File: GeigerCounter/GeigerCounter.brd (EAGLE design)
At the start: 100 x 80 mm, 0 parts

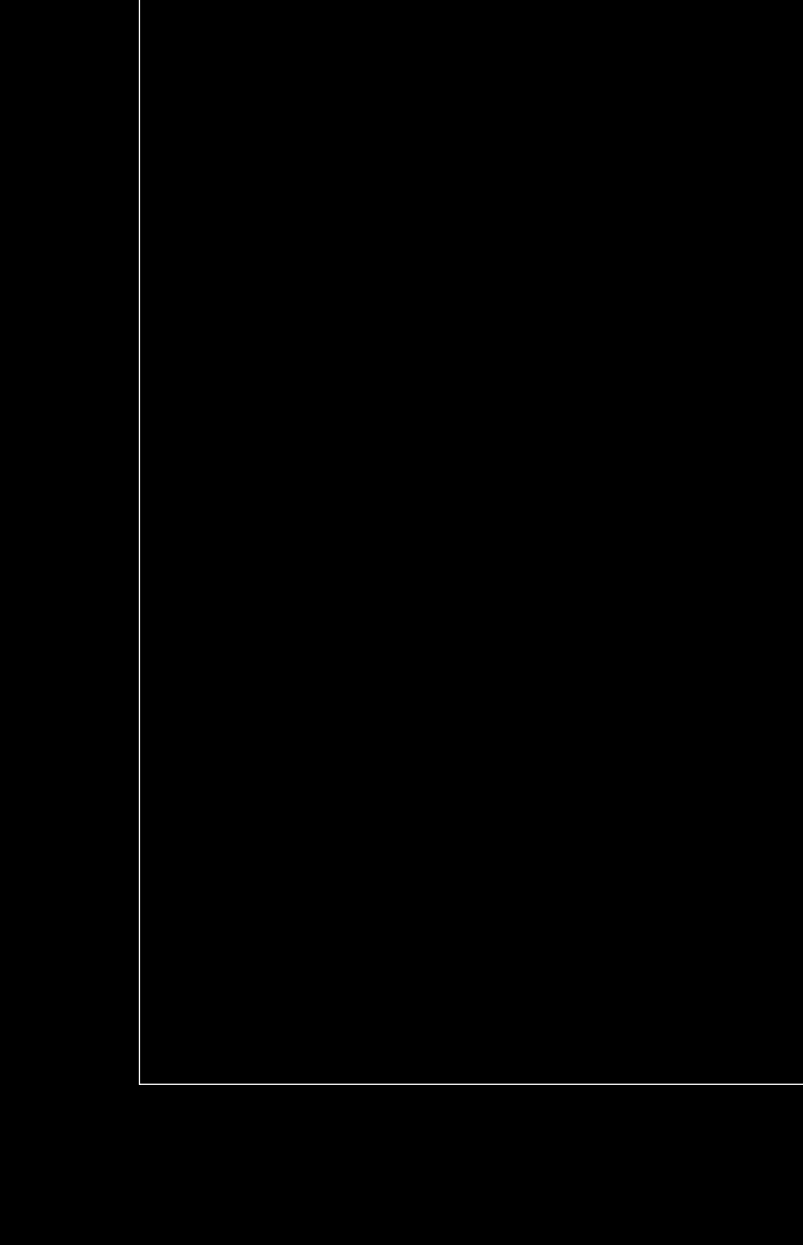
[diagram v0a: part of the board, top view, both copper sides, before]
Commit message: Added components and libraries that will be used in the project. I am using a generic op amp footprint, but made a custom photodiode footprint. I am using through hole caps and resistors throughout.
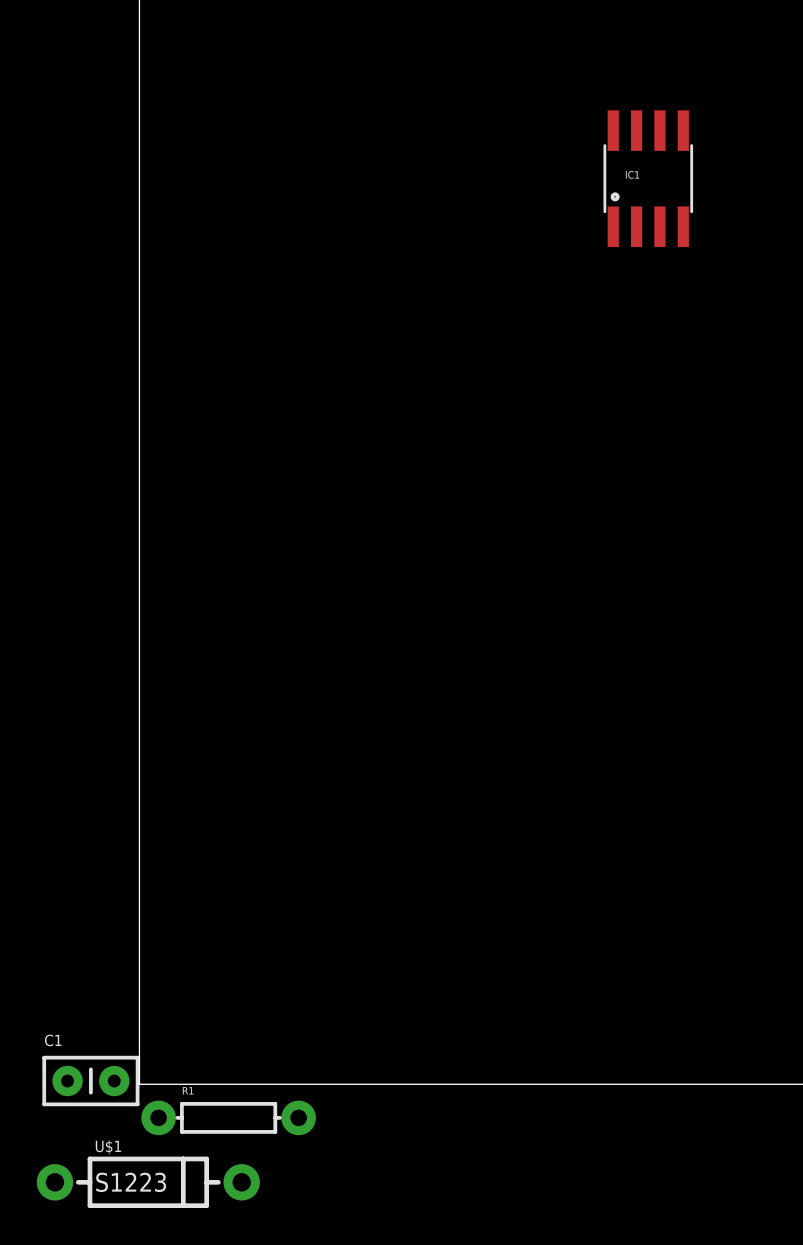
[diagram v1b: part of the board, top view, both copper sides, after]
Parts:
- added C1: (no value), SparkFun-Passives:CAP-PTH-SMALL2
- added IC1: OPAMP-DUALU, SparkFun-AnalogIC:SO08
- added R1: (no value), SparkFun-Passives:AXIAL-0.3
- added U$1: S1223, GeigerCounter:DIODE-1N4001
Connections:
- new net V+: IC1.8
- new net V-: IC1.4
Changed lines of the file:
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@@
 <setting verticaltext="up"/>
 </settings>
-<grid distance="0.05" unitdist="inch" unit="inch" style="lines" multiple="1" display="no" altdistance="0.025" altunitdist="inch" altunit="inch"/>
+<grid distance="0.001" unitdist="inch" unit="inch" style="lines" multiple="1" display="yes" altdistance="0.025" altunitdist="inch" altunit="inch"/>
 <layers>
 <layer number="1" name="Top" color="4" fill="1" visible="yes" active="yes"/>
@@
 <layer number="48" name="Document" color="7" fill="1" visible="yes" active="yes"/>
 <layer number="49" name="Reference" color="7" fill="1" visible="yes" active="yes"/>
+<layer number="50" name="dxf" color="7" fill="1" visible="no" active="no"/>
 <layer number="51" name="tDocu" color="7" fill="1" visible="yes" active="yes"/>
 <layer number="52" name="bDocu" color="7" fill="1" visible="yes" active="yes"/>
+<layer number="53" name="tGND_GNDA" color="7" fill="9" visible="no" active="no"/>
+<layer number="54" name="bGND_GNDA" color="1" fill="9" visible="no" active="no"/>
+<layer number="56" name="wert" color="7" fill="1" visible="no" active="no"/>
 <layer number="91" name="Nets" color="2" fill="1" visible="no" active="no"/>
 <layer number="92" name="Busses" color="1" fill="1" visible="no" active="no"/>
@@
 <layer number="97" name="Info" color="7" fill="1" visible="no" active="no"/>
 <layer number="98" name="Guide" color="6" fill="1" visible="no" active="no"/>
+<layer number="100" name="Muster" color="7" fill="1" visible="no" active="no"/>
+<layer number="101" name="Patch_Top" color="12" fill="4" visible="no" active="yes"/>
+<layer number="102" name="Vscore" color="7" fill="1" visible="no" active="yes"/>
+<layer number="103" name="tMap" color="7" fill="1" visible="no" active="yes"/>
+<layer number="104" name="Name" color="16" fill="1" visible="no" active="yes"/>
+<layer number="105" name="tPlate" color="7" fill="1" visible="no" active="yes"/>
+<layer number="106" name="bPlate" color="7" fill="1" visible="no" active="yes"/>
+<layer number="107" name="Crop" color="7" fill="1" visible="no" active="yes"/>
+<layer number="108" name="tplace-old" color="10" fill="1" visible="yes" active="yes"/>
+<layer number="109" name="ref-old" color="11" fill="1" visible="yes" active="yes"/>
+<layer number="116" name="Patch_BOT" color="9" fill="4" visible="no" active="yes"/>
+<layer number="121" name="_tsilk" color="7" fill="1" visible="no" active="yes"/>
+<layer number="122" name="_bsilk" color="7" fill="1" visible="no" active="yes"/>
+<layer number="125" name="_tNames" color="7" fill="1" visible="no" active="yes"/>
+<layer number="144" name="Drill_legend" color="7" fill="1" visible="no" active="yes"/>
+<layer number="151" name="HeatSink" color="7" fill="1" visible="no" active="yes"/>
+<layer number="199" name="Contour" color="7" fill="1" visible="yes" active="yes"/>
+<layer number="200" name="200bmp" color="1" fill="10" visible="no" active="yes"/>
+<layer number="201" name="201bmp" color="2" fill="10" visible="no" active="yes"/>
+<layer number="202" name="202bmp" color="3" fill="10" visible="no" active="yes"/>
+<layer number="203" name="203bmp" color="4" fill="10" visible="no" active="yes"/>
+<layer number="204" name="204bmp" color="5" fill="10" visible="no" active="yes"/>
+<layer number="205" name="205bmp" color="6" fill="10" visible="no" active="yes"/>
+<layer number="206" name="206bmp" color="7" fill="10" visible="no" active="yes"/>
+<layer number="207" name="207bmp" color="8" fill="10" visible="no" active="yes"/>
+<layer number="208" name="208bmp" color="9" fill="10" visible="no" active="yes"/>
+<layer number="209" name="209bmp" color="7" fill="1" visible="no" active="yes"/>
+<layer number="210" name="210bmp" color="7" fill="1" visible="no" active="yes"/>
+<layer number="211" name="211bmp" color="7" fill="1" visible="no" active="yes"/>
+<layer number="212" name="212bmp" color="7" fill="1" visible="no" active="yes"/>
+<layer number="213" name="213bmp" color="7" fill="1" visible="no" active="yes"/>
+<layer number="214" name="214bmp" color="7" fill="1" visible="no" active="yes"/>
+<layer number="215" name="215bmp" color="7" fill="1" visible="no" active="yes"/>
+<layer number="216" name="216bmp" color="7" fill="1" visible="no" active="yes"/>
+<layer number="217" name="217bmp" color="18" fill="1" visible="no" active="no"/>
+<layer number="218" name="218bmp" color="19" fill="1" visible="no" active="no"/>
+<layer number="219" name="219bmp" color="20" fill="1" visible="no" active="no"/>
+<layer number="220" name="220bmp" color="21" fill="1" visible="no" active="no"/>
+<layer number="221" name="221bmp" color="22" fill="1" visible="no" active="no"/>
+<layer number="222" name="222bmp" color="23" fill="1" visible="no" active="no"/>
+<layer number="223" name="223bmp" color="24" fill="1" visible="no" active="no"/>
+<layer number="224" name="224bmp" color="25" fill="1" visible="no" active="no"/>
+<layer number="250" name="Descript" color="3" fill="1" visible="no" active="no"/>
+<layer number="251" name="SMDround" color="12" fill="11" visible="no" active="no"/>
+<layer number="254" name="cooling" color="7" fill="1" visible="no" active="yes"/>
 </layers>
 <board>
@@
 </autorouter>
 <elements>
+<element name="IC1" library="SparkFun-AnalogIC" package="SO08" value="OPAMP-DUALU" x="27.686" y="49.276"/>
+<element name="R1" library="SparkFun-Passives" package="AXIAL-0.3" value="" x="4.8514" y="-1.8288"/>
+<element name="C1" library="SparkFun-Passives" package="CAP-PTH-SMALL2" value="" x="-3.9116" y="0.1778"/>
+<element name="U$1" library="GeigerCounter" package="DIODE-1N4001" value="S1223" x="0.4826" y="-5.334"/>
 </elements>
 <signals>
+<signal name="V+">
+<contactref element="IC1" pad="8"/>
+</signal>
+<signal name="V-">
+<contactref element="IC1" pad="4"/>
+</signal>
 </signals>
 </board>

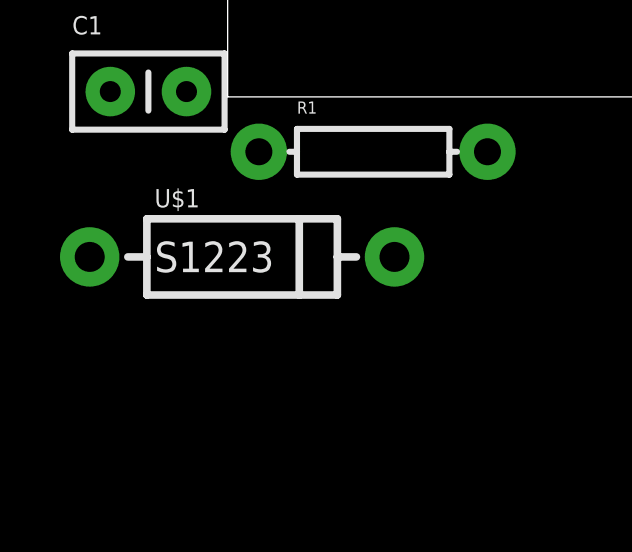
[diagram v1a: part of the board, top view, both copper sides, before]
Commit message: Added a new library part for the connector I will be using.
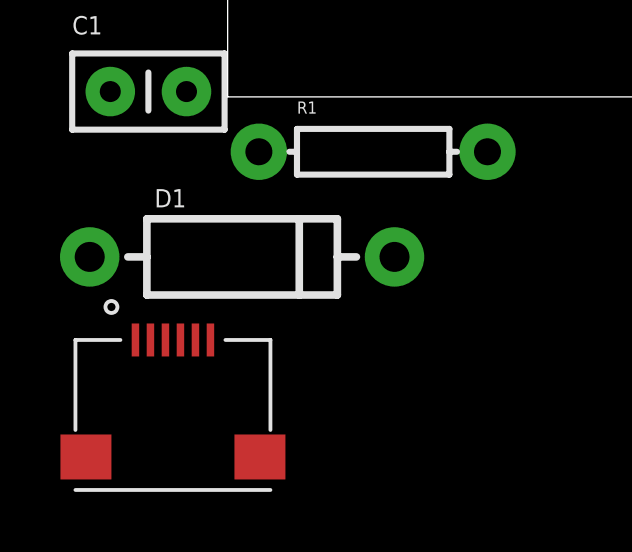
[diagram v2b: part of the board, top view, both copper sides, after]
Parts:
- added D1: S1223, GeigerCounter:DIODE-1N4001
- U$1: value S1223 -> XF2M-0615-1A; device GeigerCounter:DIODE-1N4001 -> GeigerCounter:XF2M-0615-1A
- moved U$1 5.78 mm to (-1.80, -10.6)
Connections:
- new net GND: U$1.6, U$1.P$7, U$1.P$8
- new net P3.4: U$1.5
- new net P3.5: U$1.3
- new net VCC: U$1.1
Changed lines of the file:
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@@
 <layer number="19" name="Unrouted" color="6" fill="1" visible="yes" active="yes"/>
 <layer number="20" name="Dimension" color="15" fill="1" visible="yes" active="yes"/>
-<layer number="21" name="tPlace" color="7" fill="1" visible="yes" active="yes"/>
+<layer number="21" name="tPlace" color="14" fill="1" visible="yes" active="yes"/>
 <layer number="22" name="bPlace" color="7" fill="1" visible="yes" active="yes"/>
 <layer number="23" name="tOrigins" color="15" fill="1" visible="yes" active="yes"/>
@@
 <element name="R1" library="SparkFun-Passives" package="AXIAL-0.3" value="" x="4.8514" y="-1.8288"/>
 <element name="C1" library="SparkFun-Passives" package="CAP-PTH-SMALL2" value="" x="-3.9116" y="0.1778"/>
-<element name="U$1" library="GeigerCounter" package="DIODE-1N4001" value="S1223" x="0.4826" y="-5.334"/>
+<element name="D1" library="GeigerCounter" package="DIODE-1N4001" value="S1223" x="0.4826" y="-5.334"/>
+<element name="U$1" library="GeigerCounter" package="XF2M-0615-1A" value="XF2M-0615-1A" x="-1.8034" y="-10.6426"/>
 </elements>
 <signals>
@@
 <contactref element="IC1" pad="4"/>
 </signal>
+<signal name="VCC">
+<contactref element="U$1" pad="1"/>
+</signal>
+<signal name="GND">
+<contactref element="U$1" pad="6"/>
+<contactref element="U$1" pad="P$8"/>
+<contactref element="U$1" pad="P$7"/>
+<wire x1="-0.5734" y1="-8.1026" x2="-4.7234" y2="-12.0026" width="0" layer="19" extent="1-1"/>
+<wire x1="1.0766" y1="-12.0026" x2="-0.5734" y2="-8.1026" width="0" layer="19" extent="1-1"/>
+</signal>
+<signal name="P3.5">
+<contactref element="U$1" pad="3"/>
+</signal>
+<signal name="P3.4">
+<contactref element="U$1" pad="5"/>
+</signal>
 </signals>
